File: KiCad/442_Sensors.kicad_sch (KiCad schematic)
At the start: 7 parts, among them U4 MS560702BA03-50, U5 LSM6DSO32TR, U6 SAM-M10Q

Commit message: finalize board
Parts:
- added D3: LED, LED_SMD:LED_0603_1608Metric, symbol Device:LED
- added R24: R_Small, Resistor_SMD:R_0603_1608Metric, symbol Device:R_Small
- C23, U6: now not fitted
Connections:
- net GND: now also R24.2
- net at U6.7 (TIMEPULSE): now also D3.2 (A)
- new net: D3.1 (K), R24.1
- no-connect marks 9 -> 8

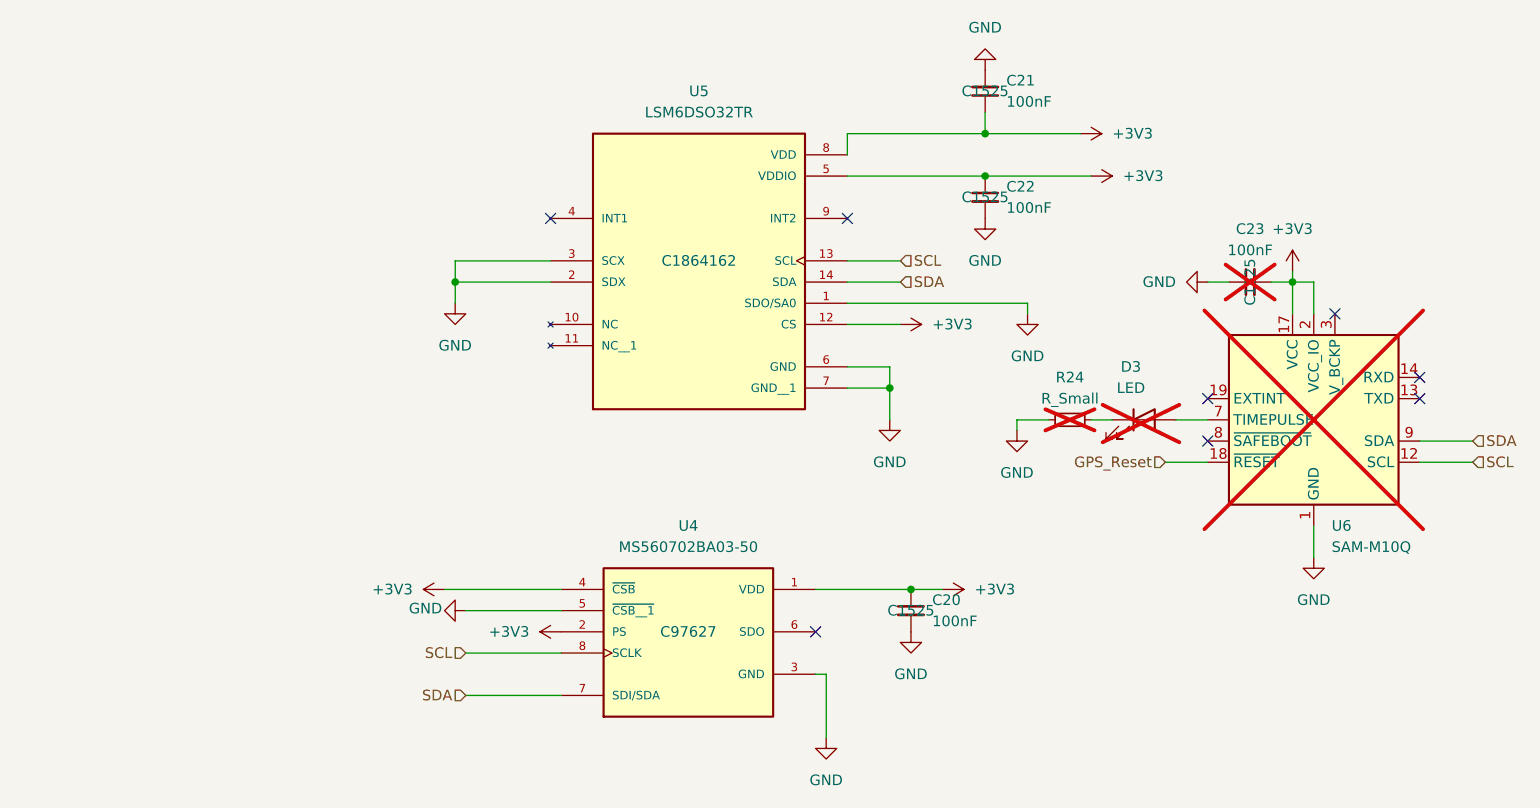
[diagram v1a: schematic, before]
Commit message: switch to BMI088 for IMU
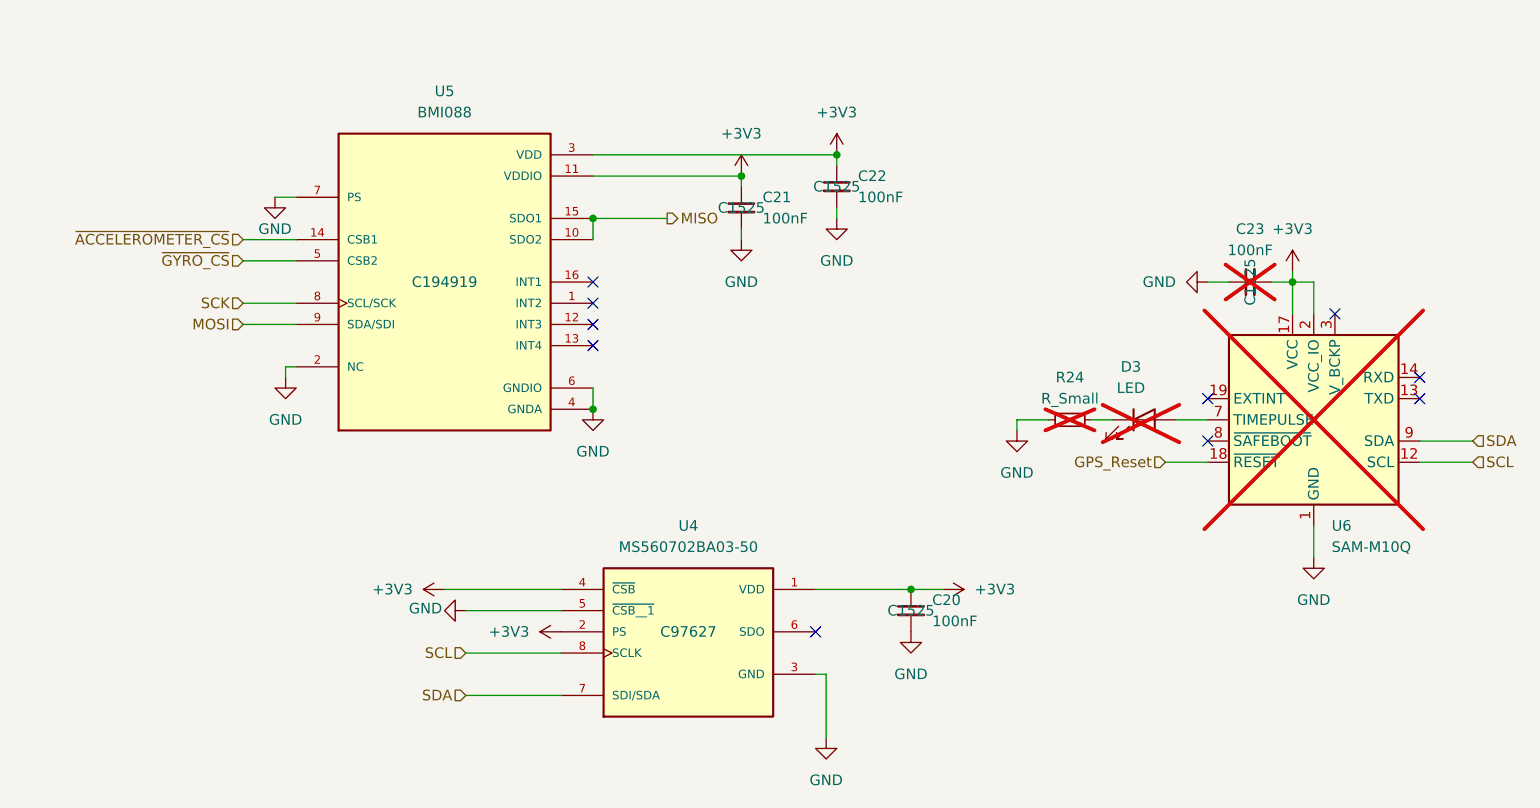
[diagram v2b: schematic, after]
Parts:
- removed U5: LSM6DSO32TR, Package_LGA:LGA-14_3x2.5mm_P0.5mm_LayoutBorder3x4y, symbol LSM6DSO32TR:LSM6DSO32TR
- added U5: BMI088, asdt-4:PQFN50P450X300X100-16N, symbol BMI088:BMI088
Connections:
- net +3V3: now also U5.11 (VDDIO), U5.3 (VDD)
- net GND: now also U5.2 (NC), U5.4 (GNDA), U5.6 (GNDIO), U5.7 (PS)
- new net MISO: U5.10 (SDO2), U5.15 (SDO1)
- new net MOSI: U5.9 (SDA/SDI)
- new net SCK: U5.8 (SCL/SCK)
- new net ~{ACCELEROMETER_CS}: U5.14 (CSB1)
- new net ~{GYRO_CS}: U5.5 (CSB2)
- no-connect marks 8 -> 10
